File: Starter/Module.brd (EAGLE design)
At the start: 25.4 x 25.4 mm, 3 parts

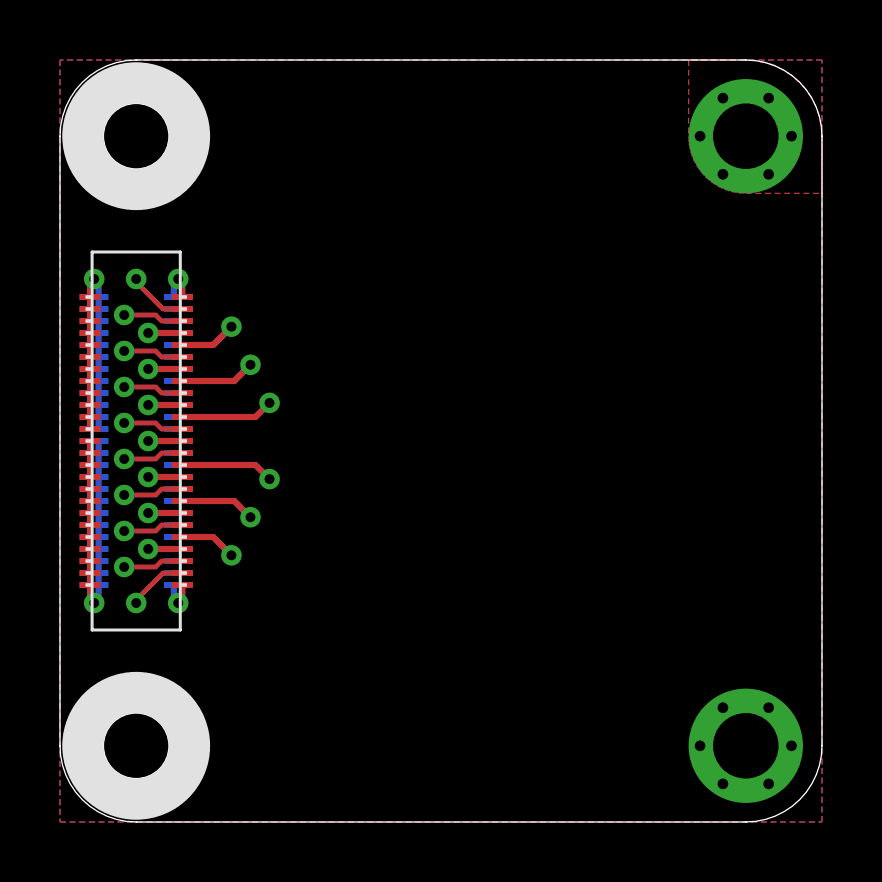
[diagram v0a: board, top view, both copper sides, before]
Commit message: Investigating idea to get rid of solder jumpers. Using LoKi Plank scheme of EEPROM and LFSF to auto-assign pins. Also moving to using two connectors instead of one for conector integrety nd module stability. EEPROM: CAT24C02 XOR: NC7S86
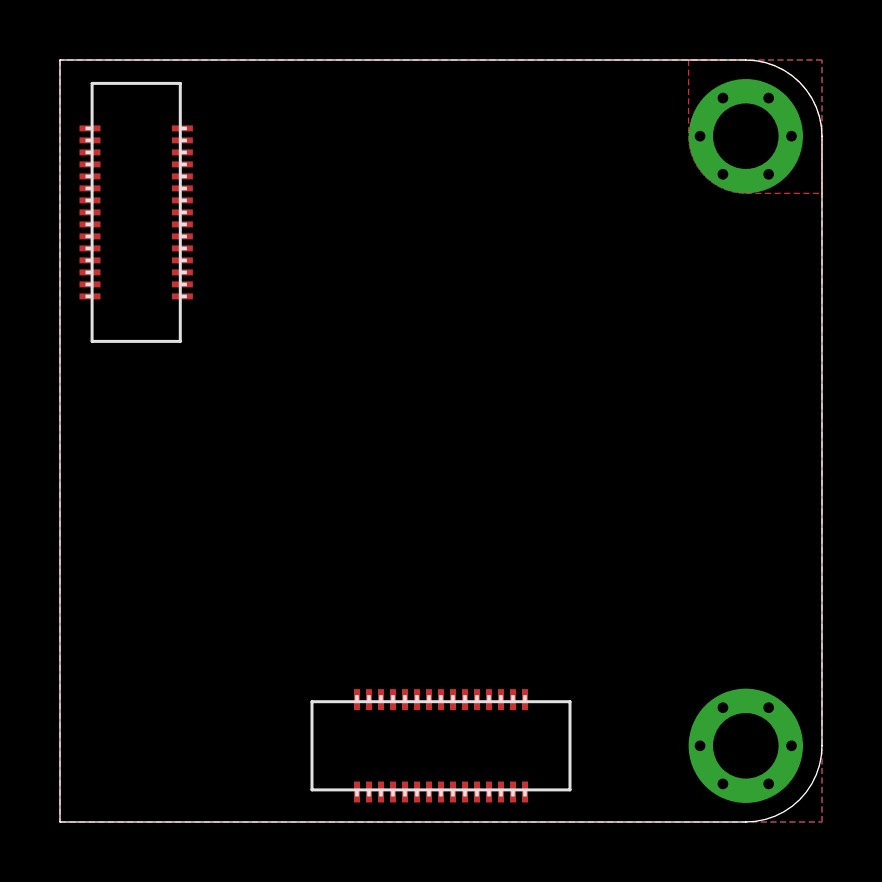
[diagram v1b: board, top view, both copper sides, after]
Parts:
- removed U$2: ROOT1.BOTH, thinkmaketest:ROOT1.BOTH
- removed U$3, U$4: HOLE.#2, .screw_holes:#2
- added U$8, U$9: DF40.30PIN.RECEPTACLE, hirose:DF40(XX)-30DS-0.4V
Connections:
- removed net 3.3V: U$2.3.3V@1, U$2.3.3V@10, U$2.3.3V@11, U$2.3.3V@12, U$2.3.3V@13, U$2.3.3V@14, U$2.3.3V@15, U$2.3.3V@16, U$2.3.3V@17, U$2.3.3V@18, U$2.3.3V@19, U$2.3.3V@2, U$2.3.3V@20, U$2.3.3V@21, U$2.3.3V@22, U$2.3.3V@23, U$2.3.3V@24, U$2.3.3V@3, U$2.3.3V@4, U$2.3.3V@5, U$2.3.3V@6, U$2.3.3V@7, U$2.3.3V@8, U$2.3.3V@9, U$2.3.3V@VIA
- removed net GND: U$2.GND@1, U$2.GND@10, U$2.GND@11, U$2.GND@12, U$2.GND@13, U$2.GND@14, U$2.GND@15, U$2.GND@16, U$2.GND@17, U$2.GND@18, U$2.GND@19, U$2.GND@2, U$2.GND@20, U$2.GND@21, U$2.GND@22, U$2.GND@23, U$2.GND@24, U$2.GND@25, U$2.GND@26, U$2.GND@3, U$2.GND@4, U$2.GND@5, U$2.GND@6, U$2.GND@7, U$2.GND@8, U$2.GND@9, U$2.GND@VIA
- removed net N$1: U$2.04, U$2.04@1, U$2.04@VIA
- removed net N$10: U$2.01, U$2.01@1, U$2.01@VIA
- removed net N$11: U$2.02, U$2.02@1, U$2.02@VIA
- removed net N$12: U$2.MOSI, U$2.MOSI@1, U$2.MOSI@VIA
- removed net N$13: U$2.ADC0, U$2.ADC0@1, U$2.ADC0@VIA
- removed net N$14: U$2.05, U$2.05@1, U$2.05@VIA
- removed net N$15: U$2.06, U$2.06@1, U$2.06@VIA
- removed net N$16: U$2.07, U$2.07@1, U$2.07@VIA
- removed net N$17: U$2.WAKE, U$2.WAKE@1, U$2.WAKE@VIA
- removed net N$18: U$2.TDI, U$2.TDI@1, U$2.TDI@VIA
- removed net N$19: U$2.TDO, U$2.TDO@1, U$2.TDO@VIA
- removed net N$2: U$2.ADC1, U$2.ADC1@1, U$2.ADC1@VIA
- removed net N$20: U$2.TCK, U$2.TCK@1, U$2.TCK@VIA
- removed net N$21: U$2.TMS, U$2.TMS@1, U$2.TMS@VIA
- removed net N$22: U$2.TRST, U$2.TRST@1, U$2.TRST@VIA
- removed net N$23: U$2.RXI.DBG, U$2.RXI.DBG@1, U$2.RXI.DBG@VIA
- removed net N$24: U$2.TXO.DBG, U$2.TXO.DBG@1, U$2.TXO.DBG@VIA
- removed net N$25: U$2.RST, U$2.RST@1, U$2.RST@VIA
- removed net N$3: U$2.SDA, U$2.SDA@1, U$2.SDA@VIA
- removed net N$4: U$2.SCL, U$2.SCL@1, U$2.SCL@VIA
- removed net N$5: U$2.03, U$2.03@1, U$2.03@VIA
- removed net N$6: U$2.MISO, U$2.MISO@1, U$2.MISO@VIA
- removed net N$7: U$2.SCLK, U$2.SCLK@1, U$2.SCLK@VIA
- removed net N$8: U$2.TXO, U$2.TXO@1, U$2.TXO@VIA
- removed net N$9: U$2.RXI, U$2.RXI@1, U$2.RXI@VIA
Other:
- outline, holes or cut-outs redrawn
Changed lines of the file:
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@@
 <?xml version="1.0" encoding="utf-8"?>
 <!DOCTYPE eagle SYSTEM "eagle.dtd">
-<eagle version="6.3">
+<eagle version="6.4">
 <drawing>
 <settings>
@@
 <layer number="23" name="tOrigins" color="15" fill="1" visible="yes" active="yes"/>
 <layer number="24" name="bOrigins" color="15" fill="1" visible="yes" active="yes"/>
-<layer number="25" name="tNames" color="7" fill="1" visible="yes" active="yes"/>
+<layer number="25" name="tNames" color="7" fill="1" visible="no" active="yes"/>
 <layer number="26" name="bNames" color="7" fill="1" visible="no" active="yes"/>
 <layer number="27" name="tValues" color="7" fill="1" visible="no" active="yes"/>
@@
 <board>
 <plain>
-<wire x1="0" y1="22.86" x2="0" y2="2.54" width="0" layer="20"/>
-<wire x1="0" y1="2.54" x2="2.54" y2="0" width="0" layer="20" curve="90"/>
-<wire x1="2.54" y1="0" x2="22.86" y2="0" width="0" layer="20"/>
+<wire x1="22.86" y1="25.4" x2="0" y2="25.4" width="0" layer="20"/>
+<wire x1="0" y1="25.4" x2="0" y2="0" width="0" layer="20"/>
+<wire x1="0" y1="0" x2="22.86" y2="0" width="0" layer="20"/>
 <wire x1="22.86" y1="0" x2="25.4" y2="2.54" width="0" layer="20" curve="90"/>
 <wire x1="25.4" y1="2.54" x2="25.4" y2="22.86" width="0" layer="20"/>
 <wire x1="25.4" y1="22.86" x2="22.86" y2="25.4" width="0" layer="20" curve="90"/>
-<wire x1="22.86" y1="25.4" x2="2.54" y2="25.4" width="0" layer="20"/>
-<wire x1="2.54" y1="25.4" x2="0" y2="22.86" width="0" layer="20" curve="90"/>
 <text x="12.7" y="1.27" size="1.016" layer="52" font="vector" ratio="12" rot="MR0" align="bottom-center">AnomalousMaker.com</text>
 <text x="12.7" y="2.54" size="1.016" layer="52" font="vector" ratio="12" rot="MR0" align="bottom-center">Cruz Monrreal II</text>
@@
 <vertex x="25.4" y="2.54"/>
 </polygon>
+<rectangle x1="1.54" y1="1.925" x2="3.54" y2="4.425" layer="51" rot="R270"/>
+<rectangle x1="4.85" y1="1.04" x2="7.85" y2="4.04" layer="51"/>
 </plain>
 <attributes>
@@
 </autorouter>
 <elements>
-<element name="U$4" library=".screw_holes" package="#2" value="HOLE.#2" x="2.54" y="22.86" rot="R90"/>
-<element name="U$3" library=".screw_holes" package="#2" value="HOLE.#2" x="2.54" y="2.54" rot="R90"/>
-<element name="U$2" library="thinkmaketest" package="ROOT1.BOTH" value="ROOT1.BOTH" x="0" y="0"/>
+<element name="U$8" library="hirose" package="DF40(XX)-30DS-0.4V" value="DF40.30PIN.RECEPTACLE" x="2.54" y="20.32" rot="R270"/>
+<element name="U$9" library="hirose" package="DF40(XX)-30DS-0.4V" value="DF40.30PIN.RECEPTACLE" x="12.7" y="2.54"/>
 </elements>
 <signals>
@@
 <vertex x="0" y="25.4"/>
 </polygon>
-<contactref element="U$2" pad="GND@12"/>
-<contactref element="U$2" pad="GND@6"/>
-<contactref element="U$2" pad="GND@10"/>
-<contactref element="U$2" pad="GND@1"/>
-<contactref element="U$2" pad="GND@11"/>
-<contactref element="U$2" pad="GND@2"/>
-<contactref element="U$2" pad="GND@7"/>
-<contactref element="U$2" pad="GND@3"/>
-<contactref element="U$2" pad="GND@5"/>
-<contactref element="U$2" pad="GND@4"/>
-<contactref element="U$2" pad="GND@13"/>
-<contactref element="U$2" pad="GND@8"/>
-<contactref element="U$2" pad="GND@9"/>
-<contactref element="U$2" pad="GND@14"/>
-<contactref element="U$2" pad="GND@15"/>
-<contactref element="U$2" pad="GND@16"/>
-<contactref element="U$2" pad="GND@17"/>
-<contactref element="U$2" pad="GND@18"/>
-<contactref element="U$2" pad="GND@19"/>
-<contactref element="U$2" pad="GND@20"/>
-<contactref element="U$2" pad="GND@21"/>
-<contactref element="U$2" pad="GND@22"/>
-<contactref element="U$2" pad="GND@23"/>
-<contactref element="U$2" pad="GND@24"/>
-<contactref element="U$2" pad="GND@25"/>
-<contactref element="U$2" pad="GND@26"/>
-<contactref element="U$2" pad="GND@VIA"/>
 <via x="22.86" y="2.54" extent="1-16" drill="2.1844" diameter="3.81"/>
 <via x="21.336" y="2.54" extent="1-16" drill="0.3556"/>
@@
 <signal name="N$30">
 </signal>
-<signal name="3.3V">
-<contactref element="U$2" pad="3.3V@5"/>
-<contactref element="U$2" pad="3.3V@3"/>
-<contactref element="U$2" pad="3.3V@2"/>
-<contactref element="U$2" pad="3.3V@4"/>
-<contactref element="U$2" pad="3.3V@10"/>
-<contactref element="U$2" pad="3.3V@8"/>
-<contactref element="U$2" pad="3.3V@9"/>
-<contactref element="U$2" pad="3.3V@6"/>
-<contactref element="U$2" pad="3.3V@7"/>
-<contactref element="U$2" pad="3.3V@11"/>
-<contactref element="U$2" pad="3.3V@1"/>
-<contactref element="U$2" pad="3.3V@12"/>
-<contactref element="U$2" pad="3.3V@13"/>
-<contactref element="U$2" pad="3.3V@14"/>
-<contactref element="U$2" pad="3.3V@15"/>
-<contactref element="U$2" pad="3.3V@16"/>
-<contactref element="U$2" pad="3.3V@17"/>
-<contactref element="U$2" pad="3.3V@18"/>
-<contactref element="U$2" pad="3.3V@19"/>
-<contactref element="U$2" pad="3.3V@20"/>
-<contactref element="U$2" pad="3.3V@21"/>
-<contactref element="U$2" pad="3.3V@22"/>
-<contactref element="U$2" pad="3.3V@23"/>
-<contactref element="U$2" pad="3.3V@24"/>
-<contactref element="U$2" pad="3.3V@VIA"/>
-</signal>
-<signal name="N$2">
-<contactref element="U$2" pad="ADC1@VIA"/>
-<contactref element="U$2" pad="ADC1@1"/>
-<contactref element="U$2" pad="ADC1"/>
-</signal>
-<signal name="N$3">
-<contactref element="U$2" pad="SDA@VIA"/>
-<contactref element="U$2" pad="SDA"/>
-<contactref element="U$2" pad="SDA@1"/>
-</signal>
-<signal name="N$4">
-<contactref element="U$2" pad="SCL@VIA"/>
-<contactref element="U$2" pad="SCL"/>
-<contactref element="U$2" pad="SCL@1"/>
-</signal>
-<signal name="N$6">
-<contactref element="U$2" pad="MISO@1"/>
-<contactref element="U$2" pad="MISO"/>
-<contactref element="U$2" pad="MISO@VIA"/>
-</signal>
-<signal name="N$7">
-<contactref element="U$2" pad="SCLK"/>
-<contactref element="U$2" pad="SCLK@1"/>
-<contactref element="U$2" pad="SCLK@VIA"/>
-</signal>
-<signal name="N$9">
-<contactref element="U$2" pad="RXI"/>
-<contactref element="U$2" pad="RXI@1"/>
-<contactref element="U$2" pad="RXI@VIA"/>
-</signal>
-<signal name="N$10">
-<contactref element="U$2" pad="01@1"/>
-<contactref element="U$2" pad="01"/>
-<contactref element="U$2" pad="01@VIA"/>
-</signal>
-<signal name="N$11">
-<contactref element="U$2" pad="02@VIA"/>
-<contactref element="U$2" pad="02"/>
-<contactref element="U$2" pad="02@1"/>
-</signal>
-<signal name="N$14">
-<contactref element="U$2" pad="05"/>
-<contactref element="U$2" pad="05@1"/>
-<contactref element="U$2" pad="05@VIA"/>
-</signal>
-<signal name="N$15">
-<contactref element="U$2" pad="06@1"/>
-<contactref element="U$2" pad="06"/>
-<contactref element="U$2" pad="06@VIA"/>
-</signal>
-<signal name="N$16">
-<contactref element="U$2" pad="07"/>
-<contactref element="U$2" pad="07@1"/>
-<contactref element="U$2" pad="07@VIA"/>
-</signal>
-<signal name="N$18">
-<contactref element="U$2" pad="TDI@1"/>
-<contactref element="U$2" pad="TDI"/>
-<contactref element="U$2" pad="TDI@VIA"/>
-</signal>
-<signal name="N$19">
-<contactref element="U$2" pad="TDO"/>
-<contactref element="U$2" pad="TDO@1"/>
-<contactref element="U$2" pad="TDO@VIA"/>
-</signal>
-<signal name="N$20">
-<contactref element="U$2" pad="TCK@1"/>
-<contactref element="U$2" pad="TCK"/>
-<contactref element="U$2" pad="TCK@VIA"/>
-</signal>
-<signal name="N$21">
-<contactref element="U$2" pad="TMS"/>
-<contactref element="U$2" pad="TMS@1"/>
-<contactref element="U$2" pad="TMS@VIA"/>
-</signal>
-<signal name="N$22">
-<contactref element="U$2" pad="TRST@1"/>
-<contactref element="U$2" pad="TRST"/>
-<contactref element="U$2" pad="TRST@VIA"/>
-</signal>
-<signal name="N$23">
-<contactref element="U$2" pad="RXI.DBG@1"/>
-<contactref element="U$2" pad="RXI.DBG"/>
-<contactref element="U$2" pad="RXI.DBG@VIA"/>
-</signal>
-<signal name="N$24">
-<contactref element="U$2" pad="TXO.DBG"/>
-<contactref element="U$2" pad="TXO.DBG@1"/>
-<contactref element="U$2" pad="TXO.DBG@VIA"/>
-</signal>
-<signal name="N$25">
-<contactref element="U$2" pad="RST@1"/>
-<contactref element="U$2" pad="RST"/>
-<contactref element="U$2" pad="RST@VIA"/>
-</signal>
-<signal name="N$5">
-<contactref element="U$2" pad="03@VIA"/>
-<contactref element="U$2" pad="03@1"/>
-<contactref element="U$2" pad="03"/>
-</signal>
-<signal name="N$8">
-<contactref element="U$2" pad="TXO@1"/>
-<contactref element="U$2" pad="TXO@VIA"/>
-<contactref element="U$2" pad="TXO"/>
-</signal>
-<signal name="N$1">
-<contactref element="U$2" pad="04@1"/>
-<contactref element="U$2" pad="04@VIA"/>
-<contactref element="U$2" pad="04"/>
-</signal>
-<signal name="N$12">
-<contactref element="U$2" pad="MOSI@1"/>
-<contactref element="U$2" pad="MOSI"/>
-<contactref element="U$2" pad="MOSI@VIA"/>
-</signal>
-<signal name="N$13">
-<contactref element="U$2" pad="ADC0@VIA"/>
-<contactref element="U$2" pad="ADC0"/>
-<contactref element="U$2" pad="ADC0@1"/>
-</signal>
-<signal name="N$17">
-<contactref element="U$2" pad="WAKE@1"/>
-<contactref element="U$2" pad="WAKE@VIA"/>
-<contactref element="U$2" pad="WAKE"/>
-</signal>
 <signal name="VIN">
